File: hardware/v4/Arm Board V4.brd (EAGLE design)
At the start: 114.3 x 50.8 mm, 51 parts, among them IC3 L6206D, U1 SN74LS241DW, U2 XBEE-1B3, U3 LSM9DS0

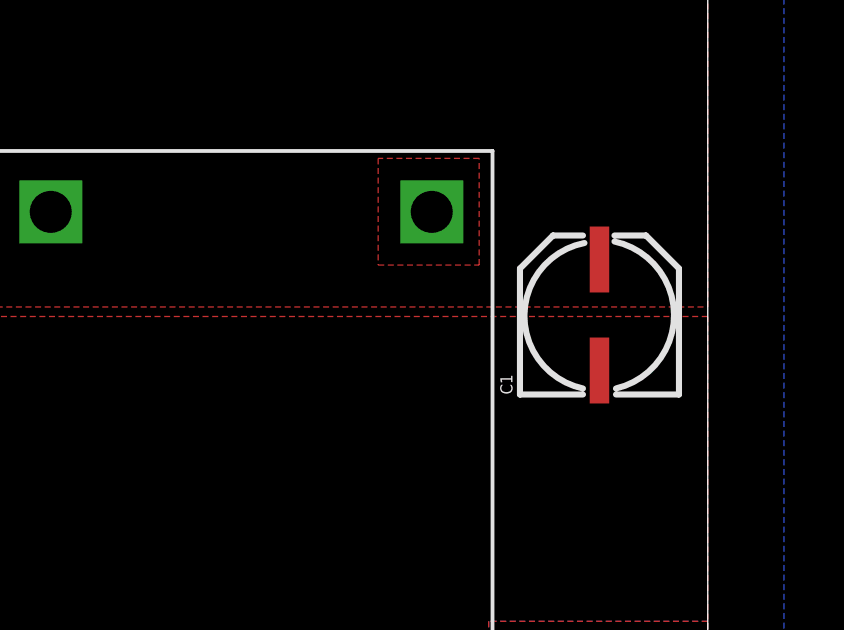
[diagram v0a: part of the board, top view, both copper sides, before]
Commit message: Readded the schematic which somehow got deleted
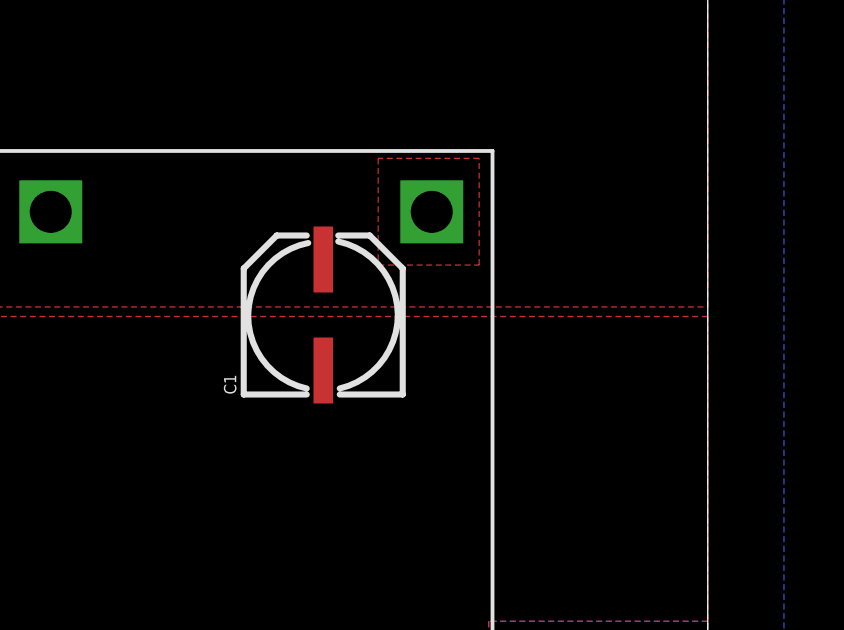
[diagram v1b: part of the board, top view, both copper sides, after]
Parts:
- moved C1 9.21 mm to (101.3, 17.5)
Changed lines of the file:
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@@
 <?xml version="1.0" encoding="utf-8"?>
 <!DOCTYPE eagle SYSTEM "eagle.dtd">
-<eagle version="6.5.0">
+<eagle version="7.1.0">
 <drawing>
 <settings>
@@
 <pass name="Default">
 <param name="RoutingGrid" value="50mil"/>
+<param name="AutoGrid" value="1"/>
+<param name="Efforts" value="0"/>
+<param name="TopRouterVariant" value="1"/>
 <param name="tpViaShape" value="round"/>
 <param name="PrefDir.1" value="|"/>
@@
 <attribute name="NAME" x="42.38625" y="38.13175" size="0.4064" layer="25" font="vector" align="bottom-center"/>
 </element>
-<element name="C1" library="SparkFun-Passives" package="PANASONIC_C" value="" x="110.49" y="17.4625" smashed="yes" rot="R90">
-<attribute name="NAME" x="107.79" y="14.8625" size="0.4064" layer="25" font="vector" rot="R90"/>
-<attribute name="VALUE" x="113.94" y="14.8625" size="0.4064" layer="27" rot="R90"/>
-</element>
+<element name="C1" library="SparkFun-Passives" package="PANASONIC_C" value="" x="101.2825" y="17.4625" rot="R90"/>
 </elements>
 <signals>

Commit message: A few things
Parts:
- moved R8 7.68 mm to (30.2, 17.1)
- moved C2 7.52 mm to (27.9, 17.1)
- moved IC3 3.86 mm to (37.5, 15.2)
- moved C12 2.54 mm to (38.7, 47.9)
- moved U$4 2.54 mm to (38.7, 43.8)
- moved R10 1.27 mm to (54.6, 42.2)
- moved R11 1.27 mm to (59.7, 42.2)
- moved R9 1.27 mm to (70.5, 35.9)
- moved U$3 1.27 mm to (57.1, 45.1)
- moved U$5 0.64 mm to (57.1, 29.8)
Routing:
- net EN_A: track 13.6 -> 21.0 mm, vias 0 -> 1
- net OCD_A: track 21.4 -> 16.3 mm, vias 3 -> 2
- net A1: track 27.0 -> 22.9 mm
- net N$3: track 19.6 -> 23.4 mm
- net N$2: track 18.2 -> 22.0 mm
- net N$1: track 23.1 -> 26.8 mm
- net A2: track 12.3 -> 8.80 mm
- net N$19: track 17.0 -> 13.5 mm
- net IN1_A: track 22.3 -> 25.5 mm
- net IN2_A: track 18.7 -> 21.9 mm
- net N$5: track 22.0 -> 25.2 mm
- net RX_3: track 105.0 -> 107.6 mm
- net TX_2: track 11.4 -> 8.84 mm
- net RX_2: track 18.6 -> 16.1 mm
- net TX_3: track 98.4 -> 100.9 mm
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
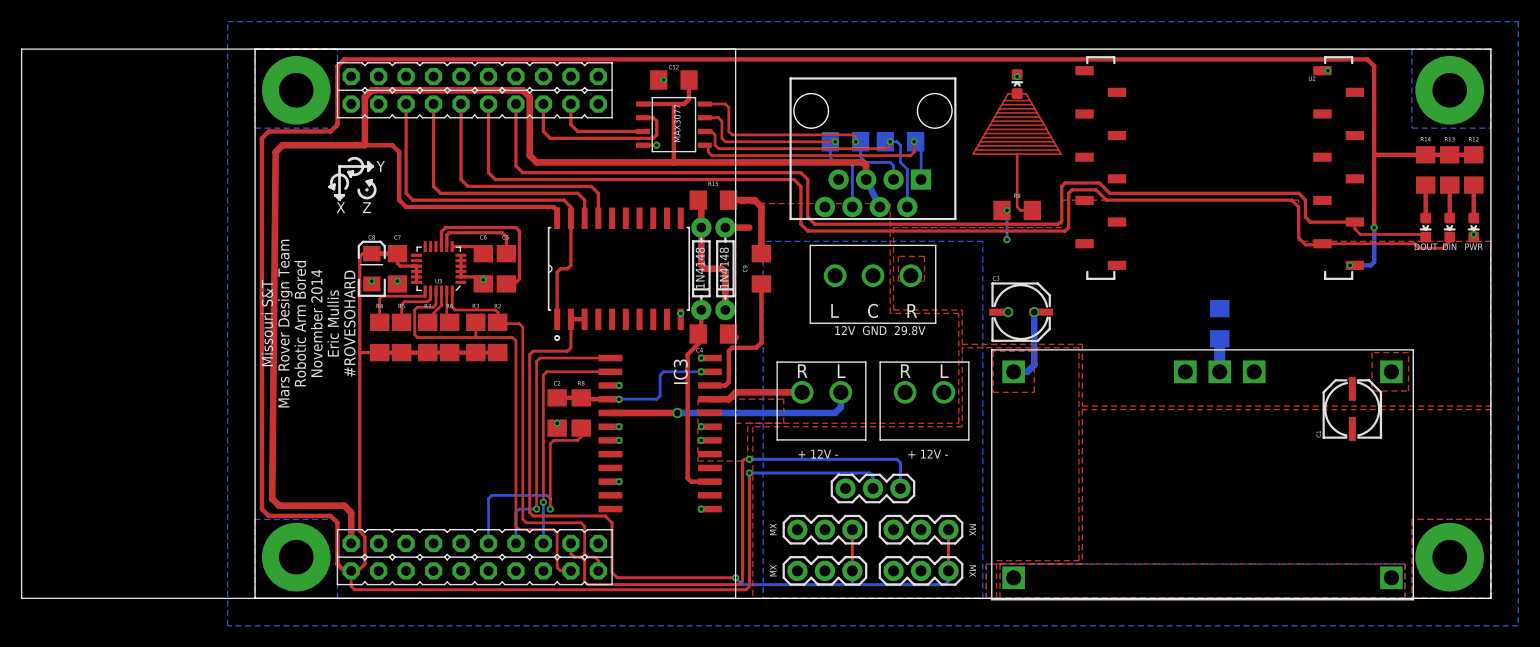
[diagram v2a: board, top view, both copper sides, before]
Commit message: Replaced caps on voltage regulator
Need to be moved into place on full eagle and cleaned up a little.  But
replaced them with ones that can be purchased rather then imaginary
ones I wished existed.
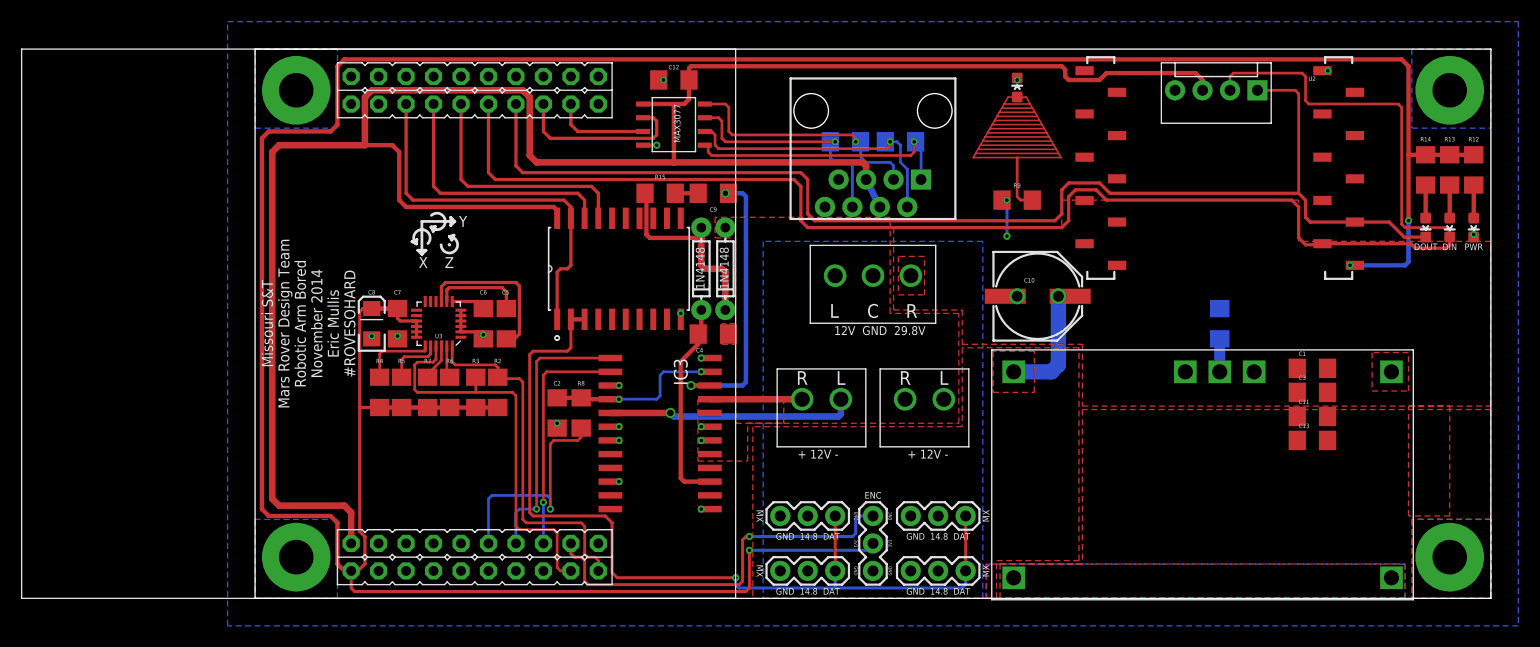
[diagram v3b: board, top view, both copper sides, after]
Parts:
- added C10: 330uF, SparkFun-Capacitors:PANASONIC_E
- added C11, C13: 4.7uF, SparkFun-Capacitors:1206
- added JP1: (no value), SparkFun-Connectors:MOLEX-1X4
- C1, C3: value (none) -> 4.7uF; device SparkFun-Passives:PANASONIC_C -> SparkFun-Capacitors:1206
- R1: value 16.5k -> 17.2k
- moved C3 28.0 mm to (97.8, 19.1)
- moved C9 8.28 mm to (42.4, 37.5), turned to 180 degrees
- moved JP7 8.03 mm to (57.1, 2.54), turned to 90 degrees
- moved C1 5.17 mm to (97.8, 21.3), turned to 0 degrees
- moved C5 5.08 mm to (23.2, 25.4)
- moved C6 5.08 mm to (21.1, 25.4)
- moved C7 5.08 mm to (13.2, 25.4)
- moved C8 5.08 mm to (10.8, 25.4)
- moved U3 5.08 mm to (17.0, 25.4)
- moved R2 5.08 mm to (22.4, 19.1)
- moved R3 5.08 mm to (20.4, 19.1)
- moved R4 5.08 mm to (11.5, 19.1)
- moved R5 5.08 mm to (13.6, 19.1)
- moved R6 5.08 mm to (18.0, 19.1)
- moved R7 5.08 mm to (16.0, 19.1)
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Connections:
- net +5V: now also JP1.3
- net 14.8V: now also C10.+; no longer C3.+
- net GND: now also C1.2, C10.-, C11.2, C13.2, C3.2, JP1.4; no longer C1.-, C3.-
- net RX_3: now also JP1.2
- net TX_3: now also JP1.1
- net VIN: now also C1.1, C11.1, C13.1, C3.1; no longer C1.+
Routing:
- net +5V: track 147.7 -> 199.1 mm
- net RX_3: track 107.6 -> 142.7 mm
- net N$19: track 13.5 -> 26.4 mm, vias 0 -> 2
- net TX_3: track 100.9 -> 112.7 mm
- net LA_ENC: track 47.6 -> 36.8 mm
- net +3V3: track 303.6 -> 293.9 mm
- net N$17: track 12.3 -> 18.5 mm
- net N$18: track 7.62 -> 2.12 mm
- net DDATA_1: track 77.3 -> 82.6 mm
- net SDA: track 38.5 -> 33.4 mm
- net SCL: track 42.5 -> 37.4 mm
- net 14.8V: track 7.81 -> 11.8 mm
- net +12V: track 3.02 -> 0.35 mm
- net N$14: track 94.7 -> 93.4 mm
- net VBOOT: track 19.2 -> 20.1 mm
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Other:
- board text added: "3V3"
- board text added: "ENC"
- board text added: "GND"
- board text added: "GND 14.8 DAT"

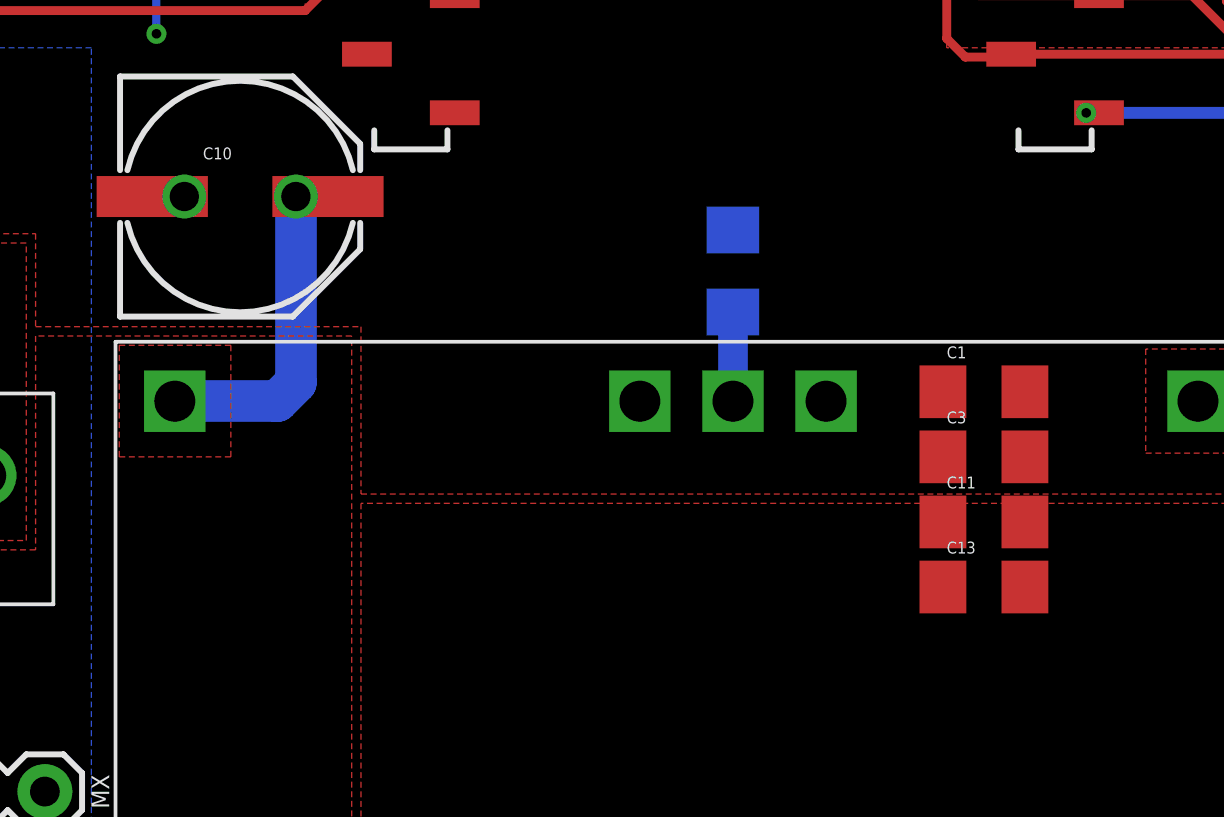
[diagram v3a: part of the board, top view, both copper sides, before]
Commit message: Added 1uF ceramic caps to help with ripple
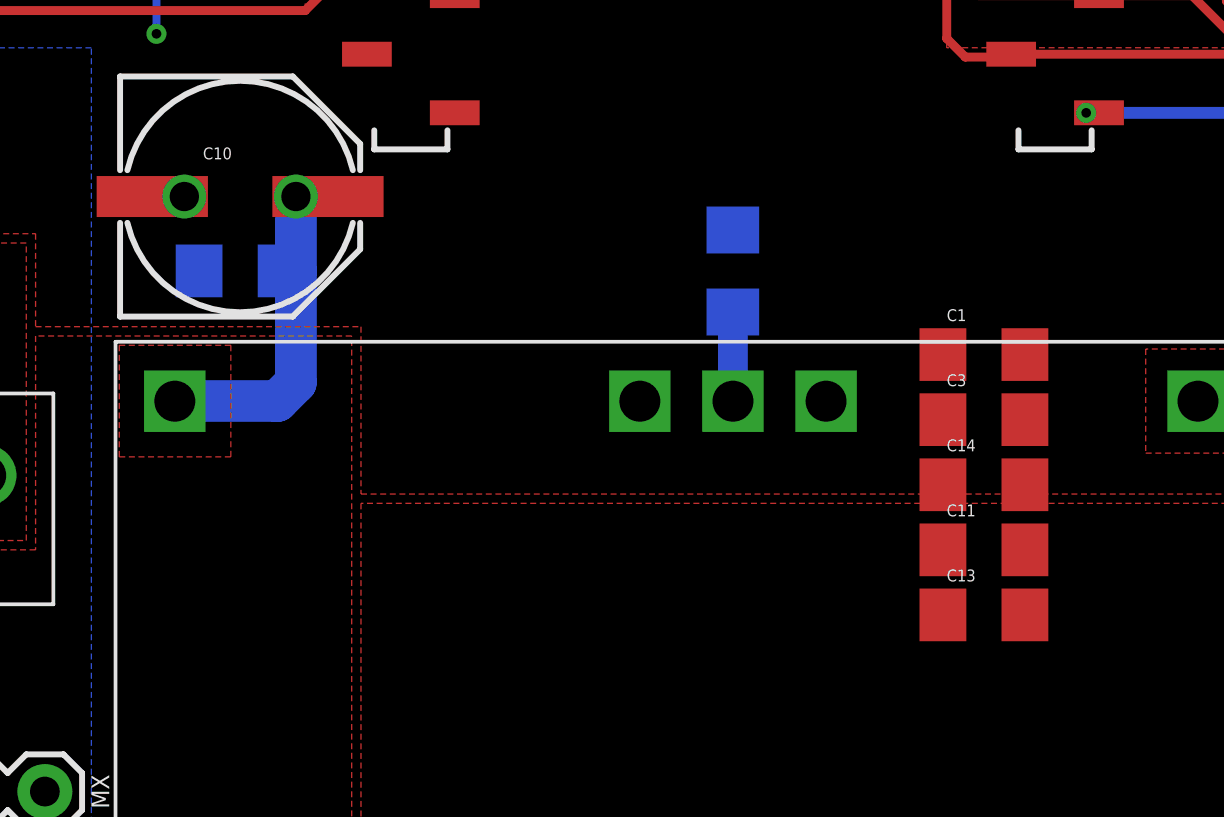
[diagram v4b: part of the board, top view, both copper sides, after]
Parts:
- added C14, C15: 1.0uF, SparkFun-Capacitors:1206
- moved C1 1.27 mm to (97.8, 22.5)
- moved C3 1.27 mm to (97.8, 20.3)
- moved C11 0.95 mm to (97.8, 15.9)
- moved C13 0.95 mm to (97.8, 13.7)
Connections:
- net 14.8V: now also C15.1
- net GND: now also C14.2, C15.2
- net VIN: now also C14.1
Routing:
- net 14.8V: track 11.8 -> 12.4 mm
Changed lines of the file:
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@@
 <element name="JP1" library="SparkFun-Connectors" package="MOLEX-1X4" value="" x="92.71" y="46.99" rot="R180"/>
 <element name="C10" library="SparkFun-Capacitors" package="PANASONIC_E" value="330uF" x="72.39" y="27.94"/>
-<element name="C1" library="SparkFun-Capacitors" package="1206" value="4.7uF" x="97.79" y="21.2725"/>
-<element name="C3" library="SparkFun-Capacitors" package="1206" value="4.7uF" x="97.79" y="19.05"/>
-<element name="C11" library="SparkFun-Capacitors" package="1206" value="4.7uF" x="97.79" y="16.8275"/>
-<element name="C13" library="SparkFun-Capacitors" package="1206" value="4.7uF" x="97.79" y="14.605"/>
+<element name="C1" library="SparkFun-Capacitors" package="1206" value="4.7uF" x="97.79" y="22.5425"/>
+<element name="C3" library="SparkFun-Capacitors" package="1206" value="4.7uF" x="97.79" y="20.32"/>
+<element name="C11" library="SparkFun-Capacitors" package="1206" value="4.7uF" x="97.79" y="15.875"/>
+<element name="C13" library="SparkFun-Capacitors" package="1206" value="4.7uF" x="97.79" y="13.6525"/>
+<element name="C14" library="SparkFun-Capacitors" package="1206" value="1.0uF" x="97.79" y="18.0975">
+<attribute name="PROD_ID" value="CAP-09822" x="97.79" y="18.0975" size="1.778" layer="27" display="off"/>
+</element>
+<element name="C15" library="SparkFun-Capacitors" package="1206" value="1.0uF" x="72.39" y="25.4" rot="MR0">
+<attribute name="PROD_ID" value="CAP-09822" x="72.39" y="25.4" size="1.778" layer="28" rot="MR0" display="off"/>
+</element>
 </elements>
 <signals>
@@
 <contactref element="C11" pad="2"/>
 <contactref element="C13" pad="2"/>
-<wire x1="99.19" y1="19.05" x2="99.19" y2="21.2725" width="0" layer="19" extent="1-1"/>
-<wire x1="99.19" y1="16.8275" x2="99.19" y2="19.05" width="0" layer="19" extent="1-1"/>
+<contactref element="C14" pad="2"/>
+<contactref element="C15" pad="2"/>
+<wire x1="99.19" y1="20.32" x2="99.19" y2="22.5425" width="0" layer="19" extent="1-1"/>
+<wire x1="99.19" y1="18.0975" x2="99.19" y2="20.32" width="0" layer="19" extent="1-1"/>
 <wire x1="69.39" y1="27.94" x2="70.485" y2="27.94" width="0" layer="19" extent="1-1"/>
 </signal>
@@
 <contactref element="C10" pad="+"/>
 <via x="74.295" y="27.94" extent="1-16" drill="1" shape="square"/>
-<wire x1="74.295" y1="27.94" x2="74.295" y2="21.59" width="1.4224" layer="16"/>
+<wire x1="74.295" y1="27.94" x2="74.295" y2="25.4" width="1.4224" layer="16"/>
+<wire x1="74.295" y1="25.4" x2="74.295" y2="21.59" width="1.4224" layer="16"/>
 <wire x1="74.295" y1="21.59" x2="73.66" y2="20.955" width="1.4224" layer="16"/>
 <wire x1="73.66" y1="20.955" x2="70.165" y2="20.955" width="1.4224" layer="16"/>
 <wire x1="70.165" y1="20.955" x2="70.16" y2="20.95" width="1.4224" layer="16"/>
 <wire x1="75.39" y1="27.94" x2="74.295" y2="27.94" width="1.27" layer="1"/>
+<contactref element="C15" pad="1"/>
+<wire x1="73.79" y1="25.4" x2="74.295" y2="25.4" width="0.4064" layer="16"/>
 </signal>
 <signal name="VIN">
@@
 <vertex x="106.68" y="17.78"/>
 </polygon>
-<wire x1="96.39" y1="14.605" x2="96.39" y2="16.8275" width="0" layer="19" extent="1-1"/>
-<wire x1="96.39" y1="19.05" x2="96.39" y2="16.8275" width="0" layer="19" extent="1-1"/>
+<contactref element="C14" pad="1"/>
+<wire x1="96.39" y1="13.6525" x2="96.39" y2="15.875" width="0" layer="19" extent="1-1"/>
+<wire x1="96.39" y1="18.0975" x2="96.39" y2="15.875" width="0" layer="19" extent="1-1"/>
 </signal>
 <signal name="RST">
